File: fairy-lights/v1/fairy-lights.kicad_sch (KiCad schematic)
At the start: 4 parts, among them J1 Conn_Coaxial_Power, J4 Screw_Terminal_01x03, Q1 IRLZ44N, U1 WeMos_D1_mini

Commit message: fix schematic
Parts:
- added R1: 10KΩ, Resistor_SMD:R_0402_1005Metric, symbol Device:R
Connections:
- net GND: now also R1.2
- net at Q1.1 (G), U1.14 (SCL/D1): now also R1.1
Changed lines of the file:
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@@
 (kicad_sch (version 20230121) (generator eeschema)
   (paper "A3")
+  (junction (at 124.46 104.14) (diameter 0) (color 0 0 0 0)
+  )
   (wire (pts (xy 171.45 91.44) (xy 171.45 135.89))
     (stroke (width 0) (type default))
@@
     (stroke (width 0) (type default))
   )
-  (wire (pts (xy 133.35 104.14) (xy 121.92 104.14))
+  (wire (pts (xy 133.35 104.14) (xy 124.46 104.14))
     (stroke (width 0) (type default))
   )
@@
     (stroke (width 0) (type default))
   )
+  (wire (pts (xy 124.46 114.3) (xy 124.46 115.57))
+    (stroke (width 0) (type default))
+  )
   (wire (pts (xy 148.59 72.39) (xy 148.59 78.74))
     (stroke (width 0) (type default))
@@
     (stroke (width 0) (type default))
   )
+  (wire (pts (xy 124.46 104.14) (xy 124.46 106.68))
+    (stroke (width 0) (type default))
+  )
   (wire (pts (xy 133.35 96.52) (xy 133.35 92.71))
     (stroke (width 0) (type default))
@@
     (stroke (width 0) (type default))
   )
-  (wire (pts (xy 114.3 109.22) (xy 114.3 114.3))
+  (wire (pts (xy 114.3 109.22) (xy 114.3 115.57))
+    (stroke (width 0) (type default))
+  )
+  (wire (pts (xy 124.46 104.14) (xy 121.92 104.14))
     (stroke (width 0) (type default))
   )
@@
     (effects (font (size 1.27 1.27)) (justify left bottom))
   )
-  (symbol (lib_id "power:GND") (at 114.3 114.3 0) (unit 1)
-    (in_bom yes) (on_board yes) (dnp no) (fields_autoplaced)
-    (property "Reference" "#PWR02" (at 114.3 120.65 0)
-      (effects (font (size 1.27 1.27)) hide)
-    )
-    (property "Value" "GND" (at 114.3 119.38 0)
-      (effects (font (size 1.27 1.27)))
-    )
-    (property "Footprint" "" (at 114.3 114.3 0)
-      (effects (font (size 1.27 1.27)) hide)
-    )
-    (property "Datasheet" "" (at 114.3 114.3 0)
+  (symbol (lib_id "power:GND") (at 114.3 115.57 0) (unit 1)
+    (in_bom yes) (on_board yes) (dnp no) (fields_autoplaced)
+    (property "Reference" "#PWR02" (at 114.3 121.92 0)
+      (effects (font (size 1.27 1.27)) hide)
+    )
+    (property "Value" "GND" (at 114.3 120.65 0)
+      (effects (font (size 1.27 1.27)))
+    )
+    (property "Footprint" "" (at 114.3 115.57 0)
+      (effects (font (size 1.27 1.27)) hide)
+    )
+    (property "Datasheet" "" (at 114.3 115.57 0)
       (effects (font (size 1.27 1.27)) hide)
     )
@@
         (path "/9e00edb4-f0f4-46bc-a82d-075ebfd0d3ed"
           (reference "#PWR01") (unit 1)
+        )
+      )
+    )
+  )
+  (symbol (lib_id "Device:R") (at 124.46 110.49 0) (unit 1)
+    (in_bom yes) (on_board yes) (dnp no)
+    (property "Reference" "R1" (at 119.38 111.76 90)
+      (effects (font (size 1.27 1.27)))
+    )
+    (property "Value" "10KΩ" (at 121.92 110.49 90)
+      (effects (font (size 1.27 1.27)))
+    )
+    (property "Footprint" "Resistor_SMD:R_0402_1005Metric" (at 122.682 110.49 90)
+      (effects (font (size 1.27 1.27)) hide)
+    )
+    (property "Datasheet" "https://datasheet.lcsc.com/lcsc/2206010100_UNI-ROYAL-Uniroyal-Elec-0402WGF1002TCE_C25744.pdf" (at 124.46 110.49 0)
+      (effects (font (size 1.27 1.27)) hide)
+    )
+    (property "LCSC" "C25744" (at 124.46 110.49 90)
+      (effects (font (size 1.27 1.27)) hide)
+    )
+    (pin "1")
+    (pin "2")
+    (instances
+      (project "fairy-lights"
+        (path "/9e00edb4-f0f4-46bc-a82d-075ebfd0d3ed"
+          (reference "R1") (unit 1)
+        )
+      )
+      (project "rgb-garden-box"
+        (path "/e63e39d7-6ac0-4ffd-8aa3-1841a4541b55"
+          (reference "R11") (unit 1)
         )
       )
@@
         )
       )
+    )
+  )
+  (symbol (lib_id "power:GND") (at 124.46 115.57 0) (unit 1)
+    (in_bom yes) (on_board yes) (dnp no) (fields_autoplaced)
+    (property "Reference" "#PWR05" (at 124.46 121.92 0)
+      (effects (font (size 1.27 1.27)) hide)
+    )
+    (property "Value" "GND" (at 124.46 120.65 0)
+      (effects (font (size 1.27 1.27)))
+    )
+    (property "Footprint" "" (at 124.46 115.57 0)
+      (effects (font (size 1.27 1.27)) hide)
+    )
+    (property "Datasheet" "" (at 124.46 115.57 0)
+      (effects (font (size 1.27 1.27)) hide)
+    )
+    (pin "1")
+    (instances
+      (project "fairy-lights"
+        (path "/9e00edb4-f0f4-46bc-a82d-075ebfd0d3ed"
+          (reference "#PWR05") (unit 1)
+        )
+      )

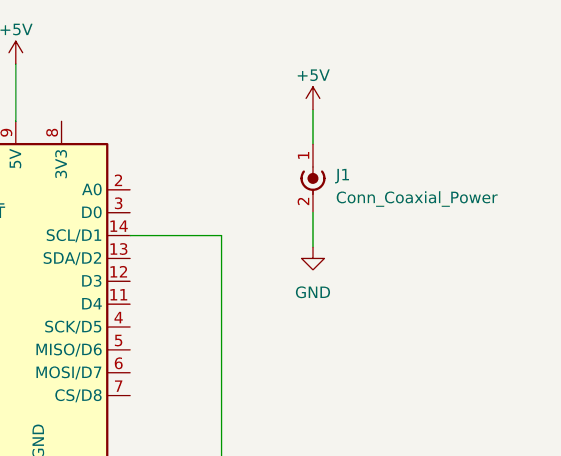
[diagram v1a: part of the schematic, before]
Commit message: finish schematic + footprints
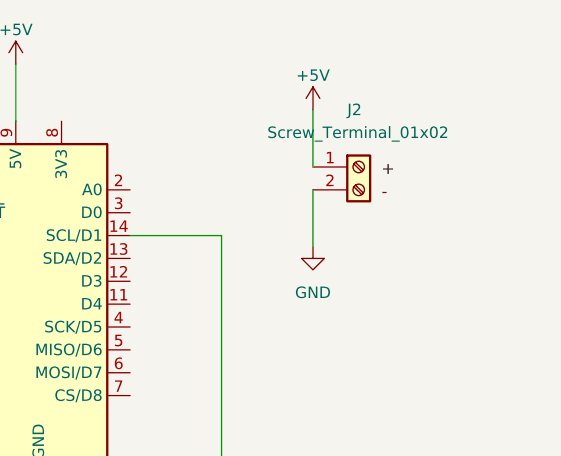
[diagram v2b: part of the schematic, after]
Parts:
- removed J1: Conn_Coaxial_Power, symbol Connector:Conn_Coaxial_Power
- added J2: Screw_Terminal_01x02, TerminalBlock:TerminalBlock_bornier-2_P5.08mm, symbol Connector:Screw_Terminal_01x02
- J4: footprint (none) -> TerminalBlock:TerminalBlock_bornier-3_P5.08mm
- R1: footprint Resistor_SMD:R_0402_1005Metric -> Resistor_THT:R_Axial_DIN0207_L6.3mm_D2.5mm_P15.24mm_Horizontal; LCSC C25744 -> (none)
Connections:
- net +5V: now also J2.1 (Pin_1)
- net GND: now also J2.2 (Pin_2)
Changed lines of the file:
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@@
     (stroke (width 0) (type default))
   )
-  (wire (pts (xy 181.61 88.9) (xy 181.61 92.71))
+  (wire (pts (xy 181.61 86.36) (xy 181.61 92.71))
     (stroke (width 0) (type default))
   )
@@
     (stroke (width 0) (type default))
   )
-  (wire (pts (xy 181.61 77.47) (xy 181.61 81.28))
+  (wire (pts (xy 181.61 77.47) (xy 181.61 83.82))
     (stroke (width 0) (type default))
   )
@@
     (stroke (width 0) (type default))
   )
+  (label "+" (at 189.23 85.09 0) (fields_autoplaced)
+    (effects (font (size 1.27 1.27)) (justify left bottom))
+  )
   (label "D" (at 99.06 93.98 0) (fields_autoplaced)
     (effects (font (size 1.27 1.27)) (justify left bottom))
   )
   (label "-" (at 99.06 96.52 0) (fields_autoplaced)
+    (effects (font (size 1.27 1.27)) (justify left bottom))
+  )
+  (label "-" (at 189.23 87.63 0) (fields_autoplaced)
     (effects (font (size 1.27 1.27)) (justify left bottom))
   )
@@
       (effects (font (size 1.27 1.27)))
     )
-    (property "Footprint" "Resistor_SMD:R_0402_1005Metric" (at 122.682 110.49 90)
-      (effects (font (size 1.27 1.27)) hide)
-    )
-    (property "Datasheet" "https://datasheet.lcsc.com/lcsc/2206010100_UNI-ROYAL-Uniroyal-Elec-0402WGF1002TCE_C25744.pdf" (at 124.46 110.49 0)
-      (effects (font (size 1.27 1.27)) hide)
-    )
-    (property "LCSC" "C25744" (at 124.46 110.49 90)
+    (property "Footprint" "Resistor_THT:R_Axial_DIN0207_L6.3mm_D2.5mm_P15.24mm_Horizontal" (at 122.682 110.49 90)
+      (effects (font (size 1.27 1.27)) hide)
+    )
+    (property "Datasheet" "" (at 124.46 110.49 0)
+      (effects (font (size 1.27 1.27)) hide)
+    )
+    (property "LCSC" "" (at 124.46 110.49 90)
       (effects (font (size 1.27 1.27)) hide)
     )
@@
       (effects (font (size 1.27 1.27)) (justify left))
     )
-    (property "Footprint" "" (at 102.87 92.71 0)
+    (property "Footprint" "TerminalBlock:TerminalBlock_bornier-3_P5.08mm" (at 102.87 92.71 0)
       (effects (font (size 1.27 1.27)) hide)
     )
@@
         (path "/9e00edb4-f0f4-46bc-a82d-075ebfd0d3ed"
           (reference "J4") (unit 1)
-        )
-      )
-    )
-  )
-  (symbol (lib_id "Connector:Conn_Coaxial_Power") (at 181.61 83.82 0) (unit 1)
-    (in_bom yes) (on_board yes) (dnp no) (fields_autoplaced)
-    (property "Reference" "J1" (at 184.15 84.709 0)
-      (effects (font (size 1.27 1.27)) (justify left))
-    )
-    (property "Value" "Conn_Coaxial_Power" (at 184.15 87.249 0)
-      (effects (font (size 1.27 1.27)) (justify left))
-    )
-    (property "Footprint" "" (at 181.61 85.09 0)
-      (effects (font (size 1.27 1.27)) hide)
-    )
-    (property "Datasheet" "~" (at 181.61 85.09 0)
-      (effects (font (size 1.27 1.27)) hide)
-    )
-    (pin "1")
-    (pin "2")
-    (instances
-      (project "fairy-lights"
-        (path "/9e00edb4-f0f4-46bc-a82d-075ebfd0d3ed"
-          (reference "J1") (unit 1)
         )
       )
@@
         )
       )
+    )
+  )
+  (symbol (lib_id "Connector:Screw_Terminal_01x02") (at 186.69 83.82 0) (unit 1)
+    (in_bom yes) (on_board yes) (dnp no)
+    (property "Reference" "J2" (at 185.42 77.47 0)
+      (effects (font (size 1.27 1.27)) (justify left))
+    )
+    (property "Value" "Screw_Terminal_01x02" (at 176.53 80.01 0)
+      (effects (font (size 1.27 1.27)) (justify left))
+    )
+    (property "Footprint" "TerminalBlock:TerminalBlock_bornier-2_P5.08mm" (at 186.69 83.82 0)
+      (effects (font (size 1.27 1.27)) hide)
+    )
+    (property "Datasheet" "~" (at 186.69 83.82 0)
+      (effects (font (size 1.27 1.27)) hide)
+    )
+    (pin "1")
+    (pin "2")
+    (instances
+      (project "fairy-lights"
+        (path "/9e00edb4-f0f4-46bc-a82d-075ebfd0d3ed"
+          (reference "J2") (unit 1)
+        )
+      )

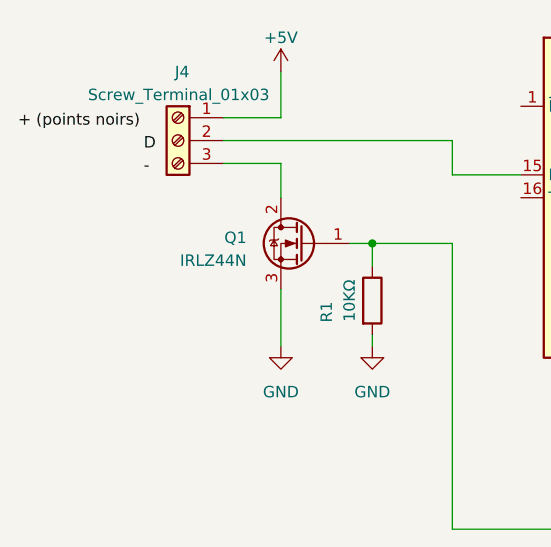
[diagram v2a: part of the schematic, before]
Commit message: Add heatsink
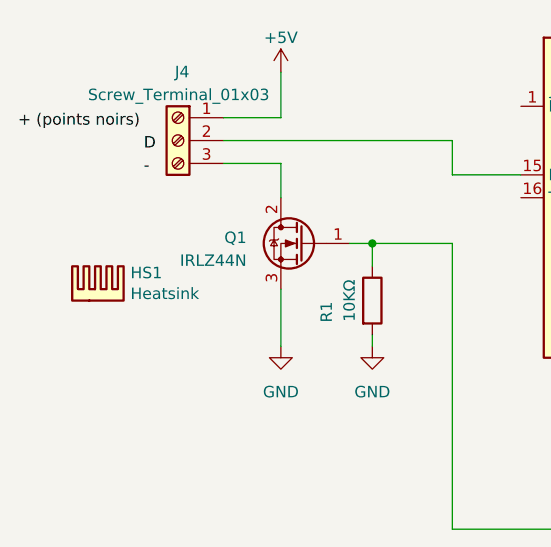
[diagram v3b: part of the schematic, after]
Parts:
- added HS1: Heatsink, Heatsink:Heatsink_Fischer_SK104-STC-STIC_35x13mm_2xDrill2.5mm, symbol Mechanical:Heatsink
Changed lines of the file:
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@@
+    )
+  )
+  (symbol (lib_id "Mechanical:Heatsink") (at 93.98 110.49 0) (unit 1)
+    (in_bom yes) (on_board yes) (dnp no)
+    (property "Reference" "HS1" (at 97.5868 107.4166 0)
+      (effects (font (size 1.27 1.27)) (justify left))
+    )
+    (property "Value" "Heatsink" (at 97.5868 109.728 0)
+      (effects (font (size 1.27 1.27)) (justify left))
+    )
+    (property "Footprint" "Heatsink:Heatsink_Fischer_SK104-STC-STIC_35x13mm_2xDrill2.5mm" (at 94.2848 110.49 0)
+      (effects (font (size 1.27 1.27)) hide)
+    )
+    (property "Datasheet" "~" (at 94.2848 110.49 0)
+      (effects (font (size 1.27 1.27)) hide)
+    )
+    (instances
+      (project "bed-smart-plug"
+        (path "/099096e4-8c2a-4d84-a16f-06b4b6330e7a"
+          (reference "HS1") (unit 1)
+        )
+      )
+      (project "fairy-lights"
+        (path "/9e00edb4-f0f4-46bc-a82d-075ebfd0d3ed"
+          (reference "HS1") (unit 1)
+        )
+      )
     )
   )
